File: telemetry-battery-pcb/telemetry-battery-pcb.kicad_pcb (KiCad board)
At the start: 2 copper layers, 94.9 x 65.1 mm, 106 parts, among them J1 Network Connector, J2 STDC14, J3 CONN_360410_MZC, J5 CONN_360410_MZC, Q1 NMOS, Q2 PMOS, Q4 NMOS, SW1 SW_Push, U1 LD39050PU33R, U2 STM32G474RBT6, U3 SN65HVD230, U4 LTC2944, U5 XR76208, U6 M24C02-WMN, U7 TPS1HTC30-Q1, Y1 8MHz

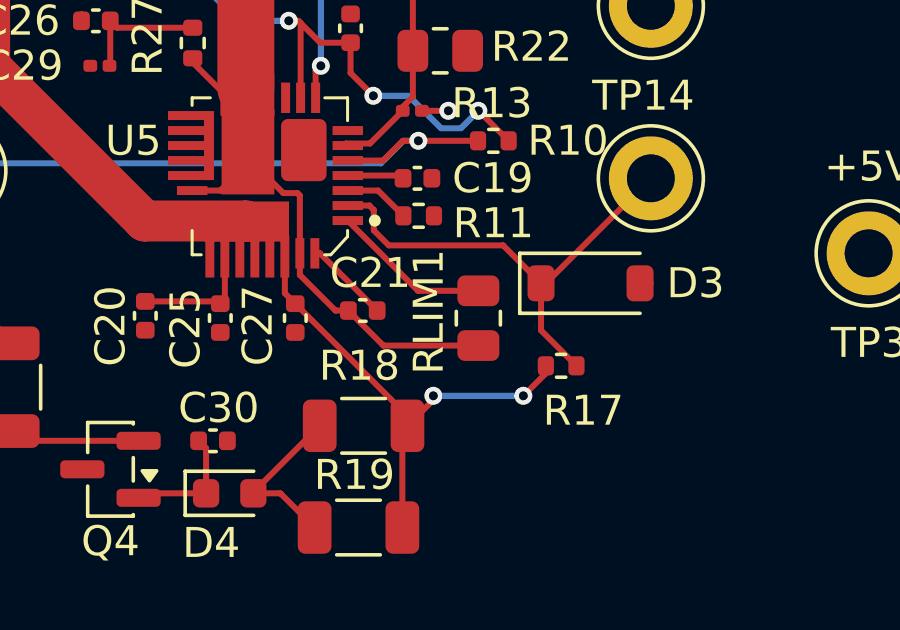
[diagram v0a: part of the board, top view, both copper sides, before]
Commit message: Telemetry-battery: Change Rlim value to 1,5k ohm based on new data
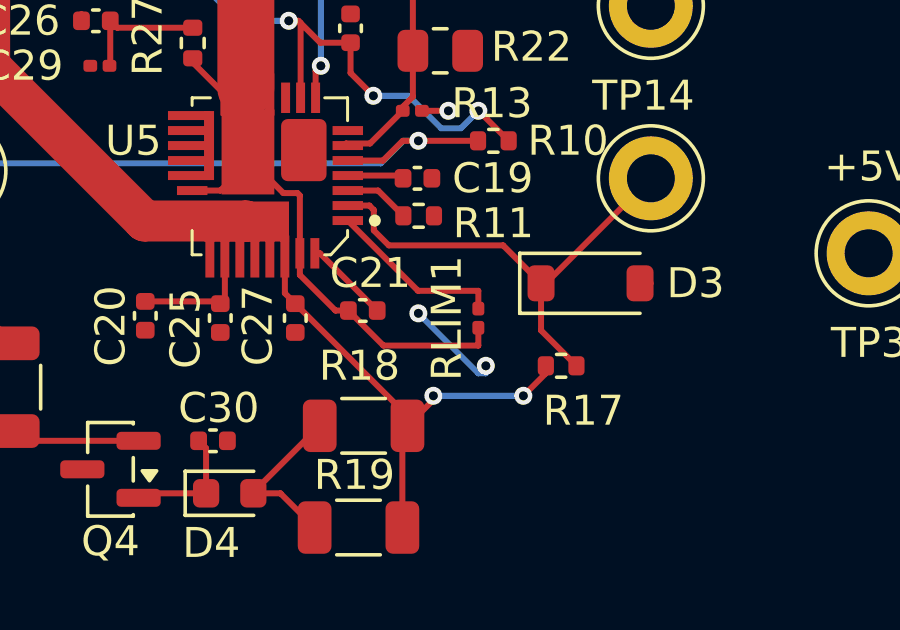
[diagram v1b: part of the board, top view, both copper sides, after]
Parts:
- RLIM1: value 4.3K -> 1.5k; footprint Resistor_SMD:R_0805_2012Metric -> Resistor_SMD:R_0201_0603Metric
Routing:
- net GND: track 1.08 -> 4.41 mm, vias 0 -> 2
- net Net-(U5-ILIM): track 5.32 -> 5.91 mm
- net /SW: track 34.6 -> 35.2 mm
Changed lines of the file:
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@@
 		)
 	)
-	(footprint "Resistor_SMD:R_0805_2012Metric"
+	(footprint "Resistor_SMD:R_0201_0603Metric"
 		(layer "F.Cu")
 		(at 117 70.9125 90)
-		(descr "Resistor SMD 0805 (2012 Metric), square (rectangular) end terminal, IPC-7351 nominal, (Body size source: IPC-SM-782 page 72, https://www.pcb-3d.com/wordpress/wp-content/uploads/ipc-sm-782a_amendment_1_and_2.pdf), generated with kicad-footprint-generator")
+		(descr "Resistor SMD 0201 (0603 Metric), square (rectangular) end terminal, IPC-7351 nominal, (Body size source: https://www.vishay.com/docs/20052/crcw0201e3.pdf), generated with kicad-footprint-generator")
 		(tags "resistor")
 		(property "Reference" "RLIM1"
-			(at 0.2125 -1.65 90)
+			(at 0 -1.05 90)
 			(layer "F.SilkS")
 			(effects
@@
 			)
 		)
-		(property "Value" "4.3K"
-			(at 0.0875 0.95 90)
+		(property "Value" "1.5k"
+			(at 0 1.05 90)
 			(layer "F.Fab")
 			(effects
@@
 			)
 		)
-		(property "JLCPCB" "C17667"
+		(property "JLCPCB" "C22843"
 			(at 0 0 90)
 			(unlocked yes)
@@
 		(attr smd)
 		(fp_line
-			(start -0.227064 -0.735)
-			(end 0.227064 -0.735)
-			(stroke
-				(width 0.12)
-				(type solid)
-			)
-			(layer "F.SilkS")
-		)
-		(fp_line
-			(start -0.227064 0.735)
-			(end 0.227064 0.735)
-			(stroke
-				(width 0.12)
-				(type solid)
-			)
-			(layer "F.SilkS")
-		)
-		(fp_line
-			(start 1.68 -0.95)
-			(end 1.68 0.95)
+			(start 0.7 -0.35)
+			(end 0.7 0.35)
 			(stroke
 				(width 0.05)
@@
 		)
 		(fp_line
-			(start -1.68 -0.95)
-			(end 1.68 -0.95)
+			(start -0.7 -0.35)
+			(end 0.7 -0.35)
 			(stroke
 				(width 0.05)
@@
 		)
 		(fp_line
-			(start 1.68 0.95)
-			(end -1.68 0.95)
+			(start 0.7 0.35)
+			(end -0.7 0.35)
 			(stroke
 				(width 0.05)
@@
 		)
 		(fp_line
-			(start -1.68 0.95)
-			(end -1.68 -0.95)
+			(start -0.7 0.35)
+			(end -0.7 -0.35)
 			(stroke
 				(width 0.05)
@@
 		)
 		(fp_line
-			(start 1 -0.625)
-			(end 1 0.625)
+			(start 0.3 -0.15)
+			(end 0.3 0.15)
 			(stroke
 				(width 0.1)
@@
 		)
 		(fp_line
-			(start -1 -0.625)
-			(end 1 -0.625)
+			(start -0.3 -0.15)
+			(end 0.3 -0.15)
 			(stroke
 				(width 0.1)
@@
 		)
 		(fp_line
-			(start 1 0.625)
-			(end -1 0.625)
+			(start 0.3 0.15)
+			(end -0.3 0.15)
 			(stroke
 				(width 0.1)
@@
 		)
 		(fp_line
-			(start -1 0.625)
-			(end -1 -0.625)
+			(start -0.3 0.15)
+			(end -0.3 -0.15)
 			(stroke
 				(width 0.1)
@@
 		)
 		(fp_text user "${REFERENCE}"
-			(at 0 0 90)
+			(at 0 -0.68 90)
 			(layer "F.Fab")
 			(effects
 				(font
-					(size 0.5 0.5)
-					(thickness 0.08)
+					(size 0.25 0.25)
+					(thickness 0.04)
 				)
 			)
 		)
+		(pad "" smd roundrect
+			(at -0.345 0 90)
+			(size 0.318 0.36)
+			(layers "F.Paste")
+			(roundrect_rratio 0.25)
+		)
+		(pad "" smd roundrect
+			(at 0.345 0 90)
+			(size 0.318 0.36)
+			(layers "F.Paste")
+			(roundrect_rratio 0.25)
+		)
 		(pad "1" smd roundrect
-			(at -0.9125 0 90)
-			(size 1.025 1.4)
-			(layers "F.Cu" "F.Mask" "F.Paste")
-			(roundrect_rratio 0.243902)
+			(at -0.32 0 90)
+			(size 0.46 0.4)
+			(layers "F.Cu" "F.Mask")
+			(roundrect_rratio 0.25)
 			(net 35 "/SW")
 			(pintype "passive")
 		)
 		(pad "2" smd roundrect
-			(at 0.9125 0 90)
-			(size 1.025 1.4)
-			(layers "F.Cu" "F.Mask" "F.Paste")
-			(roundrect_rratio 0.243902)
+			(at 0.32 0 90)
+			(size 0.46 0.4)
+			(layers "F.Cu" "F.Mask")
+			(roundrect_rratio 0.25)
 			(net 93 "Net-(U5-ILIM)")
 			(pintype "passive")
 		)
 		(embedded_fonts no)
-		(model "${KICAD9_3DMODEL_DIR}/Resistor_SMD.3dshapes/R_0805_2012Metric.step"
+		(model "${KICAD9_3DMODEL_DIR}/Resistor_SMD.3dshapes/R_0201_0603Metric.step"
 			(offset
 				(xyz 0 0 0)
@@
 		(net 1)
 	)
+	(via
+		(at 117.25 72.5)
+		(size 0.6)
+		(drill 0.3)
+		(layers "F.Cu" "B.Cu")
+		(net 1)
+	)
+	(via
+		(at 115 70.75)
+		(size 0.6)
+		(drill 0.3)
+		(layers "F.Cu" "B.Cu")
+		(free yes)
+		(net 1)
+	)
+	(segment
+		(start 117.25 72.75)
+		(end 117.25 72.5)
+		(width 0.2)
+		(layer "B.Cu")
+		(net 1)
+	)
+	(segment
+		(start 115 70.75)
+		(end 117 72.75)
+		(width 0.2)
+		(layer "B.Cu")
+		(net 1)
+	)
+	(segment
+		(start 117 72.75)
+		(end 117.25 72.75)
+		(width 0.2)
+		(layer "B.Cu")
+		(net 1)
+	)
 	(segment
 		(start 92.67 33.845)
@@
 	)
 	(segment
+		(start 117 71.2325)
+		(end 117 71.825)
+		(width 0.2)
+		(layer "F.Cu")
+		(net 35)
+	)
+	(segment
 		(start 110.5 66.742)
 		(end 109.32 65.562)
@@
 		(width 0.2)
 		(layer "F.Cu")
+		(net 93)
+	)
+	(segment
+		(start 117 70.5925)
+		(end 117 70)
+		(width 0.2)
+		(layer "F.Cu")

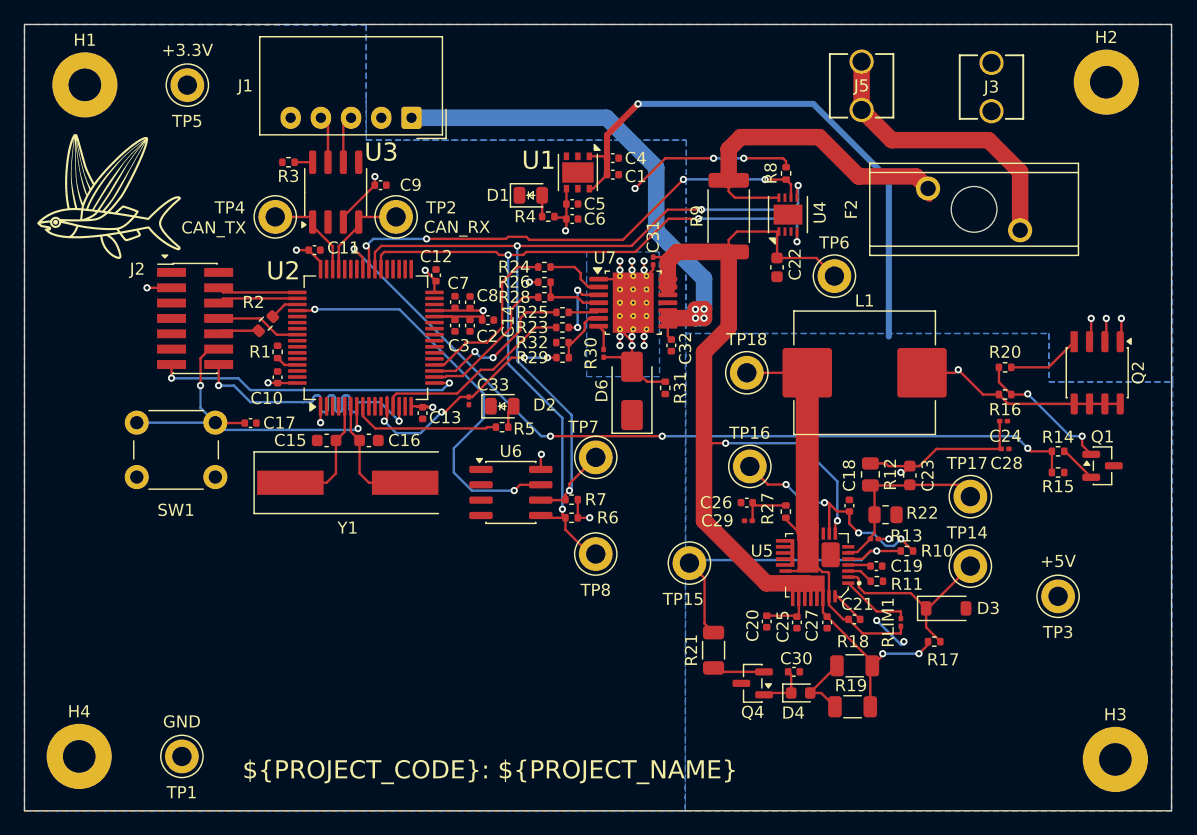
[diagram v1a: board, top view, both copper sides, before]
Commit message: telemetry-battery-pcb: add temperature sensor
Added a JST PH connector for a DS18B20 1-wire temperature sensor. Also
included the DS2484Q chip to convert 1-wire signals to i2c. All new
devices/chips powered by the +5V_net and will therefore not be
functional nor consume power before all of the network is powered on.

The i2c addresses were also added close to each chip using that
protocol to make sure there will be no conflict.
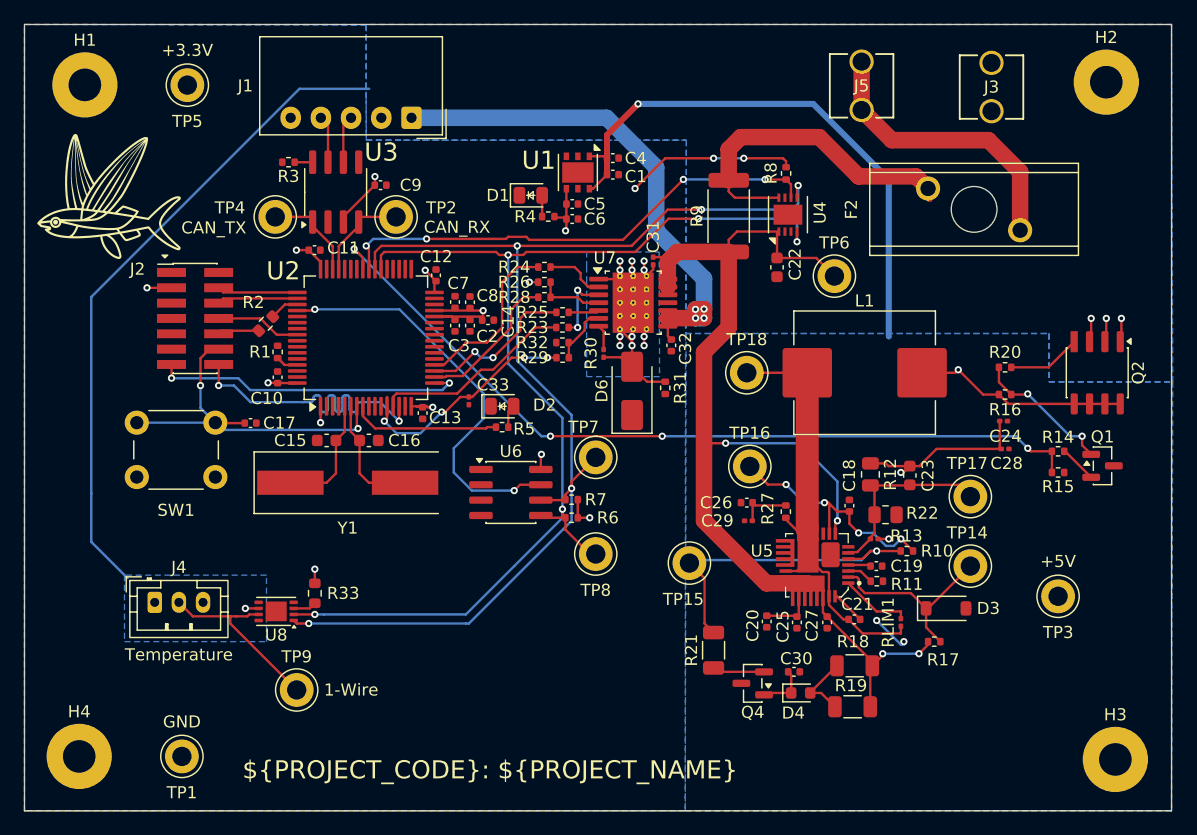
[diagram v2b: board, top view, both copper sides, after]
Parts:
- added J4: DS18B20, Connector_JST:JST_PH_B3B-PH-K_1x03_P2.00mm_Vertical, F.Cu at (55.2, 69.2)
- added R33: 2.2k, Resistor_SMD:R_0603_1608Metric, F.Cu at (68.5, 68.5)
- added TP9: TestPoint, TestPoint:TestPoint_Keystone_5005-5009_Compact, F.Cu at (67.0, 76.5)
- added U8: DS2484Q, Package_DFN_QFN:Maxim_WSON-8-1EP_3x2mm_P0.5mm_EP1.75x1.63mm, F.Cu at (65.3, 70.0)
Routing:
- net /5V_net: track 5.92 -> 61.7 mm, vias 3 -> 4
- net /SDA: track 69.5 -> 98.5 mm, vias 4 -> 5
- net /SCL: track 69.9 -> 96.1 mm, vias 4 -> 5
- net /ONE_WIRE: track 0.00 -> 15.5 mm
- net Net-(U8-~{SLPZ}): track 0.00 -> 1.93 mm
- net +3.3V: track 51.3 -> 52.4 mm, vias 15 -> 16
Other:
- board text added: "Temperature"

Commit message: telemetry-battery-pcb: move certains traces and vias
Swapped nFAULT and LATCH signals to avoid vias on one of them. Removed
90-degree corners on some traces. Move fuse for shorter traces.
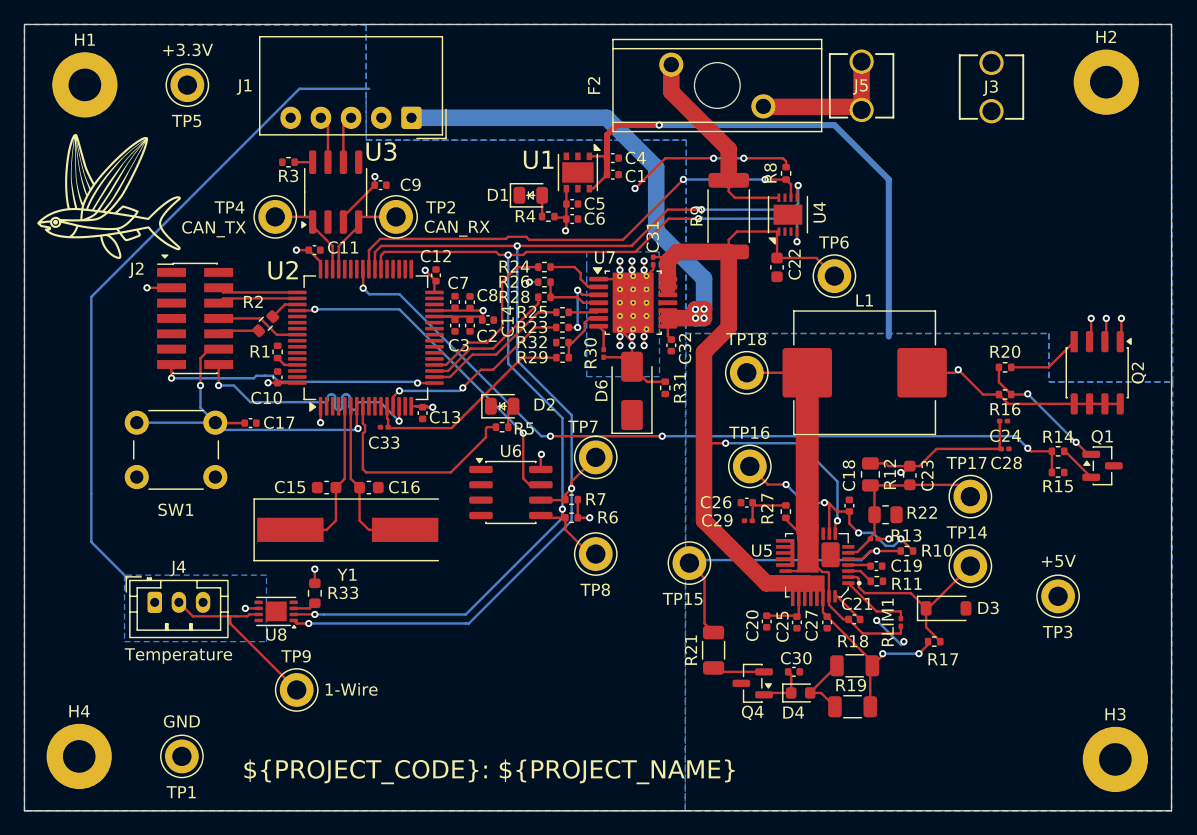
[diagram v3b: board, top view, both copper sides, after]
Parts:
- moved F2 23.6 mm to (101.8, 26.5)
- moved C33 7.33 mm to (74.2, 54.8), turned to 180 degrees
- moved C15 3.90 mm to (69.5, 59.8)
- moved C16 3.90 mm to (73.0, 59.8)
- moved Y1 3.90 mm to (71.2, 63.2)
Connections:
- U2 pad 18: /24V_nFAULT -> /24V_LATCH
- U2 pad 19: /24V_LATCH -> /24V_nFAULT
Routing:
- net /batt+: track 24.1 -> 12.3 mm
- net Net-(U4-SENSE-): track 26.8 -> 16.8 mm
- net /STM32 Base Layout/STATUS_LED: track 12.3 -> 18.5 mm
- net /EEPROM_~{WC}: track 33.9 -> 28.4 mm
- net /STM32 Base Layout/OSC_OUT: track 9.95 -> 13.8 mm
- net /STM32 Base Layout/OSC_IN: track 9.95 -> 13.8 mm
- net /STM32 Base Layout/T_VCP_RX: track 26.0 -> 23.2 mm
- net /STM32 Base Layout/T_VCP_TX: track 25.9 -> 23.1 mm
- net /open_circuit_control: track 68.4 -> 65.9 mm
- net +5V: track 80.1 -> 78.7 mm
- net /24V_SNS: track 19.5 -> 18.1 mm, vias 4 -> 0
- net /24V_LATCH: track 13.1 -> 12.3 mm, vias 2 -> 0
- net /24V_nFAULT: track 12.2 -> 11.4 mm
- net /~{ALCC}: track 41.0 -> 40.4 mm, vias 4 -> 2
- net /24V_DIAG_EN: vias 0 -> 2

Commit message: telemetry-battery-pcb: add info to silkscreen
- Added net names to test points
- Added battery polarity info
- Added fuse current
- Added PCB version
- Added connector names and reset button label
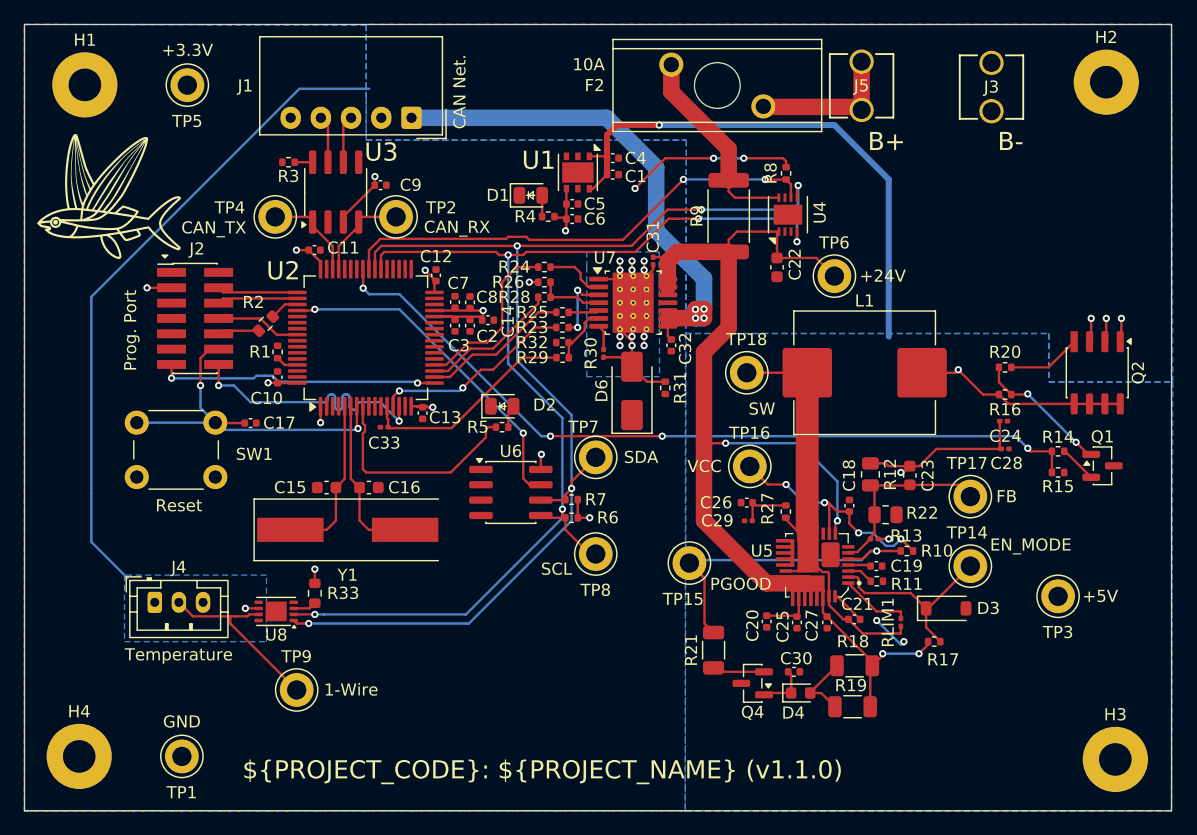
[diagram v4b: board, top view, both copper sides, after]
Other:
- board text added: "${PROJECT_CODE}: ${PROJECT_NAME} (${REVISION})"
- board text added: "B+"
- board text added: "B-"
- board text added: "CAN Net."
- board text added: "Prog. Port"
- board text added: "Reset"
- board text removed: "${PROJECT_CODE}: ${PROJECT_NAME}"
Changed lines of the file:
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@@
 	(title_block
 		(title "Base board layout")
-		(date "2025-04-06")
-		(rev "v1.0.0")
+		(date "2026-03-15")
+		(rev "v1.1.0")
 	)
 	(layers
@@
 		)
 		(property "Net Label" "SW"
-			(at 0 0 0)
+			(at 1.25 3 0)
 			(unlocked yes)
-			(layer "F.Fab")
-			(hide yes)
+			(layer "F.SilkS")
 			(effects
 				(font
@@
 		(tags "resistor")
 		(property "Reference" "R26"
-			(at -2.51 0 0)
+			(at -3 0 0)
 			(layer "F.SilkS")
 			(effects
@@
 			)
 		)
-		(property "Net Label" "VCC"
-			(at 0 0 0)
+		(property "Net Label" "+24V"
+			(at 4 0 0)
 			(unlocked yes)
-			(layer "F.Fab")
-			(hide yes)
+			(layer "F.SilkS")
 			(effects
 				(font
@@
 		(tags "Fuse")
 		(property "Reference" "F2"
-			(at 0 -10.16 90)
+			(at 0 -10.16 180)
 			(layer "F.SilkS")
 			(effects
@@
 		)
 		(property "Value" "10A"
-			(at -0.4908 -0.1082 90)
+			(at 1.7272 -9.31 180)
 			(layer "F.SilkS")
-			(hide yes)
 			(effects
 				(font
-					(size 1.27 1.27)
-					(thickness 0.254)
+					(size 1 1)
+					(thickness 0.15)
 				)
+				(justify right)
 			)
 		)
@@
 		(tags "resistor")
 		(property "Reference" "R5"
-			(at 1.83 0.145 0)
+			(at -2 0 0)
 			(layer "F.SilkS")
 			(effects
@@
 		(tags "Surface mounted pin header SMD 2x07 1.27mm double row")
 		(property "Reference" "J2"
-			(at -4.77 -4.08 0)
+			(at 0.16 -5.755 0)
 			(layer "F.SilkS")
 			(effects
@@
 		)
 		(property "Net Label" "EN_MODE"
-			(at 0 0 0)
+			(at 5 -1.75 0)
 			(unlocked yes)
-			(layer "F.Fab")
-			(hide yes)
+			(layer "F.SilkS")
 			(effects
 				(font
@@
 		)
 		(property "Net Label" "FB"
-			(at 0 0 0)
+			(at 3 0 0)
 			(unlocked yes)
-			(layer "F.Fab")
-			(hide yes)
+			(layer "F.SilkS")
 			(effects
 				(font
@@
 			)
 		)
-		(property "Net Label" "VCC"
-			(at 0 0 0)
+		(property "Net Label" "SDA"
+			(at 3.75 0 0)
 			(unlocked yes)
-			(layer "F.Fab")
-			(hide yes)
+			(layer "F.SilkS")
 			(effects
 				(font
@@
 			)
 		)
-		(property "Net Label" "VCC"
-			(at 0 0 0)
+		(property "Net Label" "SCL"
+			(at -3.25 1.25 0)
 			(unlocked yes)
-			(layer "F.Fab")
-			(hide yes)
+			(layer "F.SilkS")
 			(effects
 				(font
@@
 		)
 		(property "Net Label" "PGOOD"
-			(at 0 0 0)
+			(at 4.25 1.75 0)
 			(unlocked yes)
-			(layer "F.Fab")
-			(hide yes)
+			(layer "F.SilkS")
 			(effects
 				(font
@@
 		(tags "tact sw push 6mm")
 		(property "Reference" "SW1"
-			(at 3.25 7.25 0)
+			(at 9.735 2.62 0)
 			(layer "F.SilkS")
 			(effects
@@
 		)
 		(property "Net Label" "VCC"
-			(at 0 0 0)
+			(at -3.75 0 0)
 			(unlocked yes)
-			(layer "F.Fab")
-			(hide yes)
+			(layer "F.SilkS")
 			(effects
 				(font
@@
 		)
 		(property "Net Label" "+5V"
-			(at 0 -2.89 0)
+			(at 3.49 0 0)
 			(unlocked yes)
 			(layer "F.SilkS")
@@
 		(tags "capacitor")
 		(property "Reference" "C8"
-			(at 0.55 1.45 180)
+			(at 0.415 1.41 180)
 			(layer "F.SilkS")
 			(effects
@@
 		(layer "Edge.Cuts")
 	)
+	(gr_text "Prog. Port"
+		(at 53.25 46.75 90)
+		(layer "F.SilkS")
+		(effects
+			(font
+				(size 1 1)
+				(thickness 0.15)
+			)
+		)
+	)
+	(gr_text "Reset"
+		(at 57.25 61.25 0)
+		(layer "F.SilkS")
+		(effects
+			(font
+				(size 1 1)
+				(thickness 0.15)
+			)
+		)
+	)
 	(gr_text "Temperature"
 		(at 57.25 73 0)
@@
 			(font
 				(size 1 1)
-				(thickness 0.1)
+				(thickness 0.15)
 			)
 			(justify top)
 		)
 	)
-	(gr_text "${PROJECT_CODE}: ${PROJECT_NAME}"
+	(gr_text "B-"
+		(at 125 32 0)
+		(layer "F.SilkS")
+		(effects
+			(font
+				(size 1.5 1.5)
+				(thickness 0.175)
+			)
+			(justify left bottom)
+		)
+	)
+	(gr_text "CAN Net."
+		(at 80.5 27 90)
+		(layer "F.SilkS")
+		(effects
+			(font
+				(size 1 1)
+				(thickness 0.15)
+			)
+		)
+	)
+	(gr_text "${PROJECT_CODE}: ${PROJECT_NAME} (${REVISION})"
 		(at 62.5 84 0)
 		(layer "F.SilkS")
@@
 			)
 			(justify left bottom)
+		)
+	)
+	(gr_text "B+"
+		(at 114.25 32 0)
+		(layer "F.SilkS")
+		(effects
+			(font
+				(size 1.5 1.5)
+				(thickness 0.175)
+			)
+			(justify left bottom)
